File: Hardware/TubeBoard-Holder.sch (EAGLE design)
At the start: 24 parts, among them T1 MPSA42, T2 MPSA42

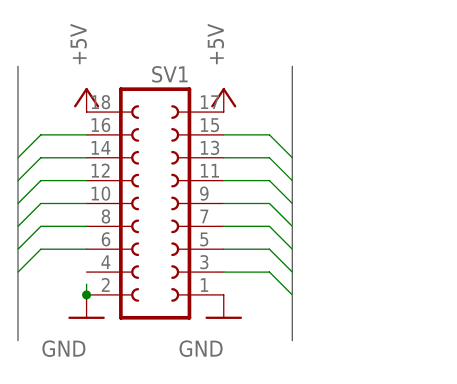
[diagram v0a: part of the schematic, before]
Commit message: added ARM chip to driver boards to PWM tubes
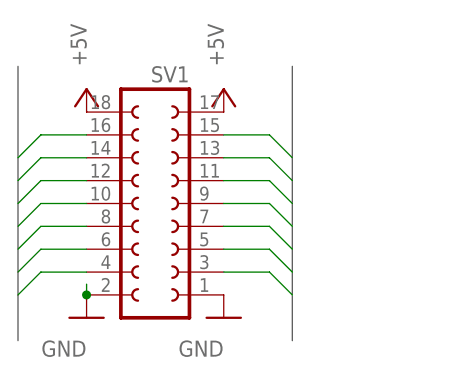
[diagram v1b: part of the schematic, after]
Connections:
- net DRIVE_HI renamed PWM2
- net DRIVE_LO renamed PWM0
- net DRIVE_MED renamed PWM1
- net N$7 renamed PWM3
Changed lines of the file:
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@@
 </segment>
 </bus>
-<bus name="COLON_B,COLON_T,DRIVE_HI,DRIVE_LO,DRIVE_MED,LDIGIT[0..3],RDIGIT[0..3]">
+<bus name="COLON_B,COLON_T,DRIVE[0..3],LDIGIT[0..3],RDIGIT[0..3]">
+<segment>
+<wire x1="35.56" y1="35.56" x2="35.56" y2="5.08" width="0.762" layer="92"/>
+</segment>
 <segment>
 <wire x1="5.08" y1="35.56" x2="5.08" y2="5.08" width="0.762" layer="92"/>
-</segment>
-<segment>
-<wire x1="35.56" y1="35.56" x2="35.56" y2="5.08" width="0.762" layer="92"/>
 </segment>
 </bus>
@@
 </segment>
 </net>
-<net name="DRIVE_LO" class="0">
+<net name="PWM0" class="0">
 <segment>
 <wire x1="27.94" y1="17.78" x2="33.02" y2="17.78" width="0.1524" layer="91"/>
@@
 </segment>
 </net>
-<net name="DRIVE_MED" class="0">
+<net name="PWM1" class="0">
 <segment>
 <wire x1="27.94" y1="15.24" x2="33.02" y2="15.24" width="0.1524" layer="91"/>
@@
 </segment>
 </net>
-<net name="DRIVE_HI" class="0">
+<net name="PWM2" class="0">
 <segment>
 <wire x1="27.94" y1="12.7" x2="33.02" y2="12.7" width="0.1524" layer="91"/>
@@
 </segment>
 </net>
-<net name="N$7" class="0">
-<segment>
-<wire x1="12.7" y1="12.7" x2="12.7" y2="12.7" width="0.1524" layer="91"/>
-<pinref part="SV1" gate="1" pin="4"/>
-</segment>
-</net>
 <net name="N$8" class="0">
 <segment>
@@
 </segment>
 </net>
+<net name="PWM3" class="0">
+<segment>
+<pinref part="SV1" gate="1" pin="4"/>
+<wire x1="5.08" y1="10.16" x2="7.62" y2="12.7" width="0.1524" layer="91"/>
+<wire x1="7.62" y1="12.7" x2="12.7" y2="12.7" width="0.1524" layer="91"/>
+</segment>
+</net>

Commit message: added pwm drivers to tube board
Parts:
- added OC1, OC2, OC3, OC4: PC-LTV352T, we-opto:PC-LTV352T
- added R10, R11, R8, R9: 330R, rcl:R-EU_R2012
- R3, R4: value 174k -> 105k; MOUSER 667-ERJ-8ENF1743V -> 667-ERJ-8ENF1053V
- R5, R6: value 15k -> 9k1; MOUER 588-OM1535E-R58 -> 588-OM9125E-R58
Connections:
- new net 1_ANODE: OC1.TE, R5.2
- new net 2_ANODE: OC2.TE, R6.2
- new net B_ANODE: OC3.TE, R4.1
- new net N$10: OC2.A, R9.2
- new net N$12: OC3.A, R10.2
- new net N$14: OC4.A, R11.2
- new net N$7: OC1.A, R8.2
- new net T_ANODE: OC4.TE, R3.1
- net +5V: now also R10.1, R11.1, R8.1, R9.1
- net HV_ANODE: now also OC1.TC, OC2.TC, OC3.TC, OC4.TC; no longer R3.1, R4.1, R5.2, R6.2
- net PWM0: now also OC1.C
- net PWM1: now also OC2.C
- net PWM2: now also OC3.C
- net PWM3: now also OC4.C
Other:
- note added: "R5/R6 should be 15k if not using PWM R3/R4 should be 174k if not using PWM"
- moved on the sheet: C1, C2
